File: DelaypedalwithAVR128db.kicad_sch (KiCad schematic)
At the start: 0 parts

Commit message: voltage bais
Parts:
- added C1: C, symbol Device:C
- added R1, R2: R, symbol Device:R
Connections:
- new net: C1.2, R1.2, R2.1
- new net Audio input: C1.1

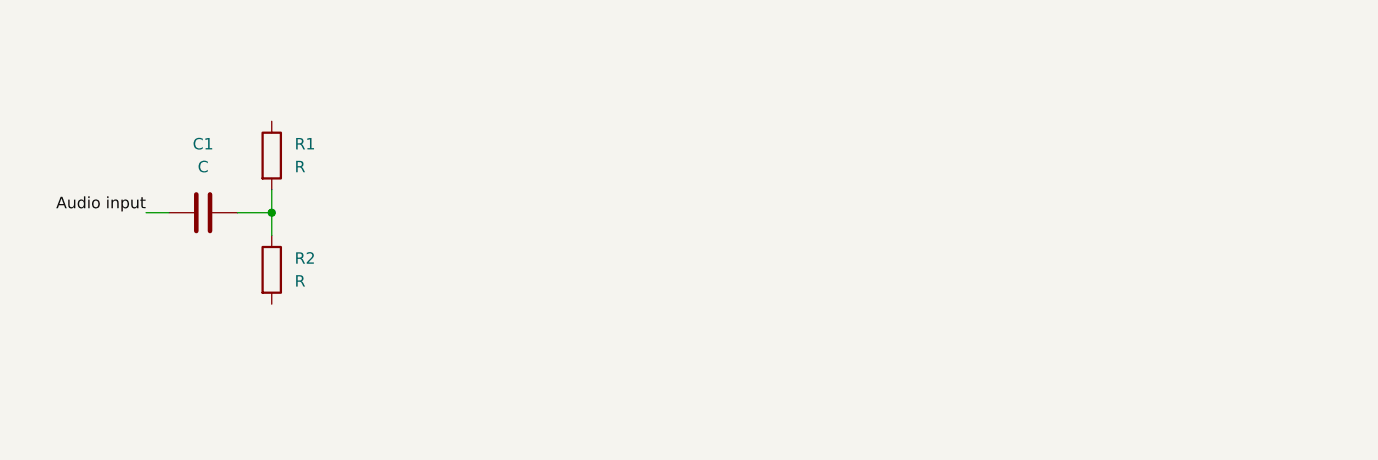
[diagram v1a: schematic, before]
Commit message: almost input stage done
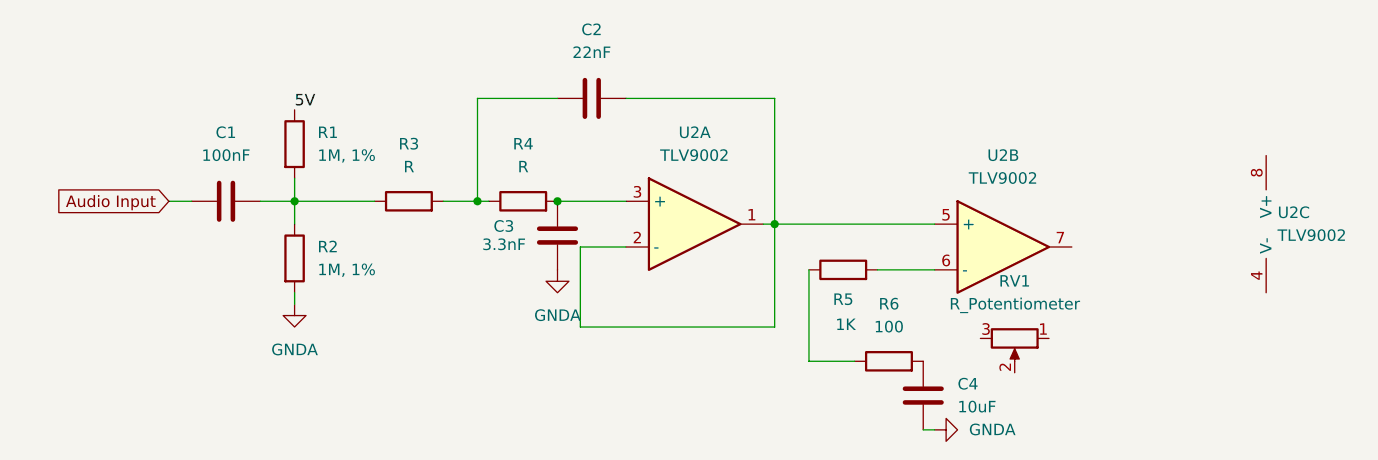
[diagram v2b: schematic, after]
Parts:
- added C2: 22nF, symbol Device:C
- added C3: 3.3nF, symbol Device:C
- added C4: 10uF, symbol Device:C
- added R3, R4: R, symbol Device:R
- added R5: 1K, symbol Device:R
- added R6: 100, symbol Device:R
- added RV1: R_Potentiometer, symbol Device:R_Potentiometer
- added U2: TLV9002, symbol Device:Opamp_Dual
- C1: value C -> 100nF
- R1, R2: value R -> 1M, 1%
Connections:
- net at C1.2, R1.2, R2.1: now also R3.1
- net 5V: now reaches R1.1
- net GNDA: now reaches R2.2
- net GNDA: now also C3.1, C4.1
- net Audio input renamed Audio Input
- new net: C2.1, R3.2, R4.1
- new net: C2.2, U2.1, U2.2 (-), U2.5 (+)
- new net: C3.2, R4.2, U2.3 (+)
- new net: C4.2, R6.2
- new net: R5.1, R6.1
- new net: R5.2, U2.6 (-)
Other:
- moved on the sheet: C1, R1, R2

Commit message: input stage finished and mixer stage
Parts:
- added C5, C6, C7, C8: 100nF, symbol Device:C
- added RV2: R_Potentiometer, symbol Device:R_Potentiometer
- added U1: TLV9002, symbol Device:Opamp_Dual
- RV1: value R_Potentiometer -> Potentiometer, 10K, linear
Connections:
- net GNDA: now also C6.2, C8.2
- net at U2.4 (V-): now also C6.1
- net at U2.8 (V+): now also C5.2
- net at R5.2, U2.6 (-): now also RV1.2, RV1.3
- net Dry positive signal: now reaches RV1.1
- net Dry positive signal: now also U2.7, RV2.1
- new net: C8.1, U1.4 (V-)
- new net: RV2.2, U1.3 (+)
- new net: C7.1, U1.8 (V+)
- new net 5VA: C5.1, C7.2
- new net Audio output: U1.1, U1.2 (-)
- new net Wet positive signal: RV2.3
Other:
- note added: "Input stage"
- note added: "Mixer"
- moved on the sheet: U2C

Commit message: fixed output maming
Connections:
- net Audio output renamed Audio ouput 1
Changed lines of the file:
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@@
+		)
+	)
+	(label "Audio ouput 1"
+		(at 66.04 127 0)
+		(effects
+			(font
+				(size 1.27 1.27)
+			)
+			(justify left bottom)
 		)
 	)
@@
 				(hide yes)
 			)
-		)
-	)
-	(global_label "Audio output"
-		(shape input)
-		(at 66.04 127 0)
-		(fields_autoplaced yes)
-		(effects
-			(font
-				(size 1.27 1.27)
-			)
-			(justify left)
-		)
-		(property "Intersheetrefs" "${INTERSHEET_REFS}"
-			(at 81.1806 127 0)
-			(effects
-				(font
-					(size 1.27 1.27)
-				)
-				(justify left)
-				(hide yes)
-			)

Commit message: added relay
yep thats it
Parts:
- added K1: Relay_SPDT, symbol Relay:Relay_SPDT
- R3, R4: value R -> 4,7K
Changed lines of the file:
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@@
 			)
 		)
-		(property "Value" "R"
+		(property "Value" "4,7K"
 			(at 54.61 69.85 90)
 			(effects
@@
 			)
 		)
-		(property "Value" "R"
+		(property "Value" "4,7K"
 			(at 67.31 69.85 90)
 			(effects
@@
 				)
 			)
+		)
+	)
+	(symbol
+		(lib_id "Relay:Relay_SPDT")
+		(at 41.91 161.29 0)
+		(unit 1)
+		(exclude_from_sim no)
+		(in_bom yes)
+		(on_board yes)
+		(dnp no)
+		(fields_autoplaced yes)
+		(property "Reference" "K1"
+			(at 53.34 160.0199 0)
+			(effects
+				(font
+					(size 1.27 1.27)
+				)
+				(justify left)
+			)
+		)
+		(property "Value" "Relay_SPDT"
+			(at 53.34 162.5599 0)
+			(effects
+				(font
+					(size 1.27 1.27)
+				)
+				(justify left)
+			)
+		)
+		(property "Footprint" ""
+			(at 53.34 162.56 0)
+			(effects
+				(font
+					(size 1.27 1.27)
+				)
+				(justify left)
+				(hide yes)
+			)
+		)
+		(property "Datasheet" "~"
+			(at 41.91 161.29 0)
+			(effects
+				(font
+					(size 1.27 1.27)
+				)
+				(hide yes)
+			)
+		)
+		(property "Description" "Relay SPDT, monostable, EN50005"
+			(at 41.91 161.29 0)
+			(effects
+				(font
+					(size 1.27 1.27)
+				)
+				(hide yes)
+			)
+		)
+		(pin "11"
+		)
+		(pin "14"
+		)
+		(pin "A1"
+		)
+		(pin "12"
+		)
+		(pin "A2"
+		)
+		(instances
+			(project ""
+				(path "/df84d36d-d6d4-4d90-9a88-48fc6a8fe70c"
+					(reference "K1")
+					(unit 1)
+				)
+			)

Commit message: bypass almost done
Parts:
- added C9: 10uF, symbol Device:C
- added J1, J2: NJ2FD-V, Connector_Audio:Jack_6.35mm_Neutrik_NJ2FD-V_Vertical, symbol Connector_Audio:NJ2FD-V
- added R7: 1M, symbol Device:R
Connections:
- net Dry positive signal: now also K1.12
- net GNDA: now also J1.S, J2.S, R7.1
- net at K1.11: now also C9.1
- net Audio output 1: now reaches K1.14
- net Audio Input renamed Audio input
- net Audio input: now also J1.T
- new net Audio outpu: C9.2, J2.T, R7.2
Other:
- note added: "Bypass"
- moved on the sheet: K1

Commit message: Bypass finished???
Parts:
- added C10: 10uF, PCM_JLCPCB:C_1206, symbol PCM_JLCPCB-Capacitors:1206,10uF
- added C11: 100nF, PCM_JLCPCB:C_1206, symbol PCM_JLCPCB-Capacitors:1206,100nF
- added D1: IN4148, symbol Device:D
- added Q1: BC847, Package_TO_SOT_SMD:SOT-23, symbol Transistor_BJT:BC847
- added R8: 1K, symbol Device:R
- added R9: 10K, symbol Device:R
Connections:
- net 5VA: now also K1.A1, C10.1, C11.1, D1.1 (K)
- net GNDA: now also C10.2, C11.2, Q1.3 (C), R9.1
- net at K1.A2: now also D1.2 (A), Q1.2 (E)
- new net: Q1.1 (B), R8.2, R9.2
- new net Bypass pin: R8.1
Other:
- moved on the sheet: C9, J2, K1

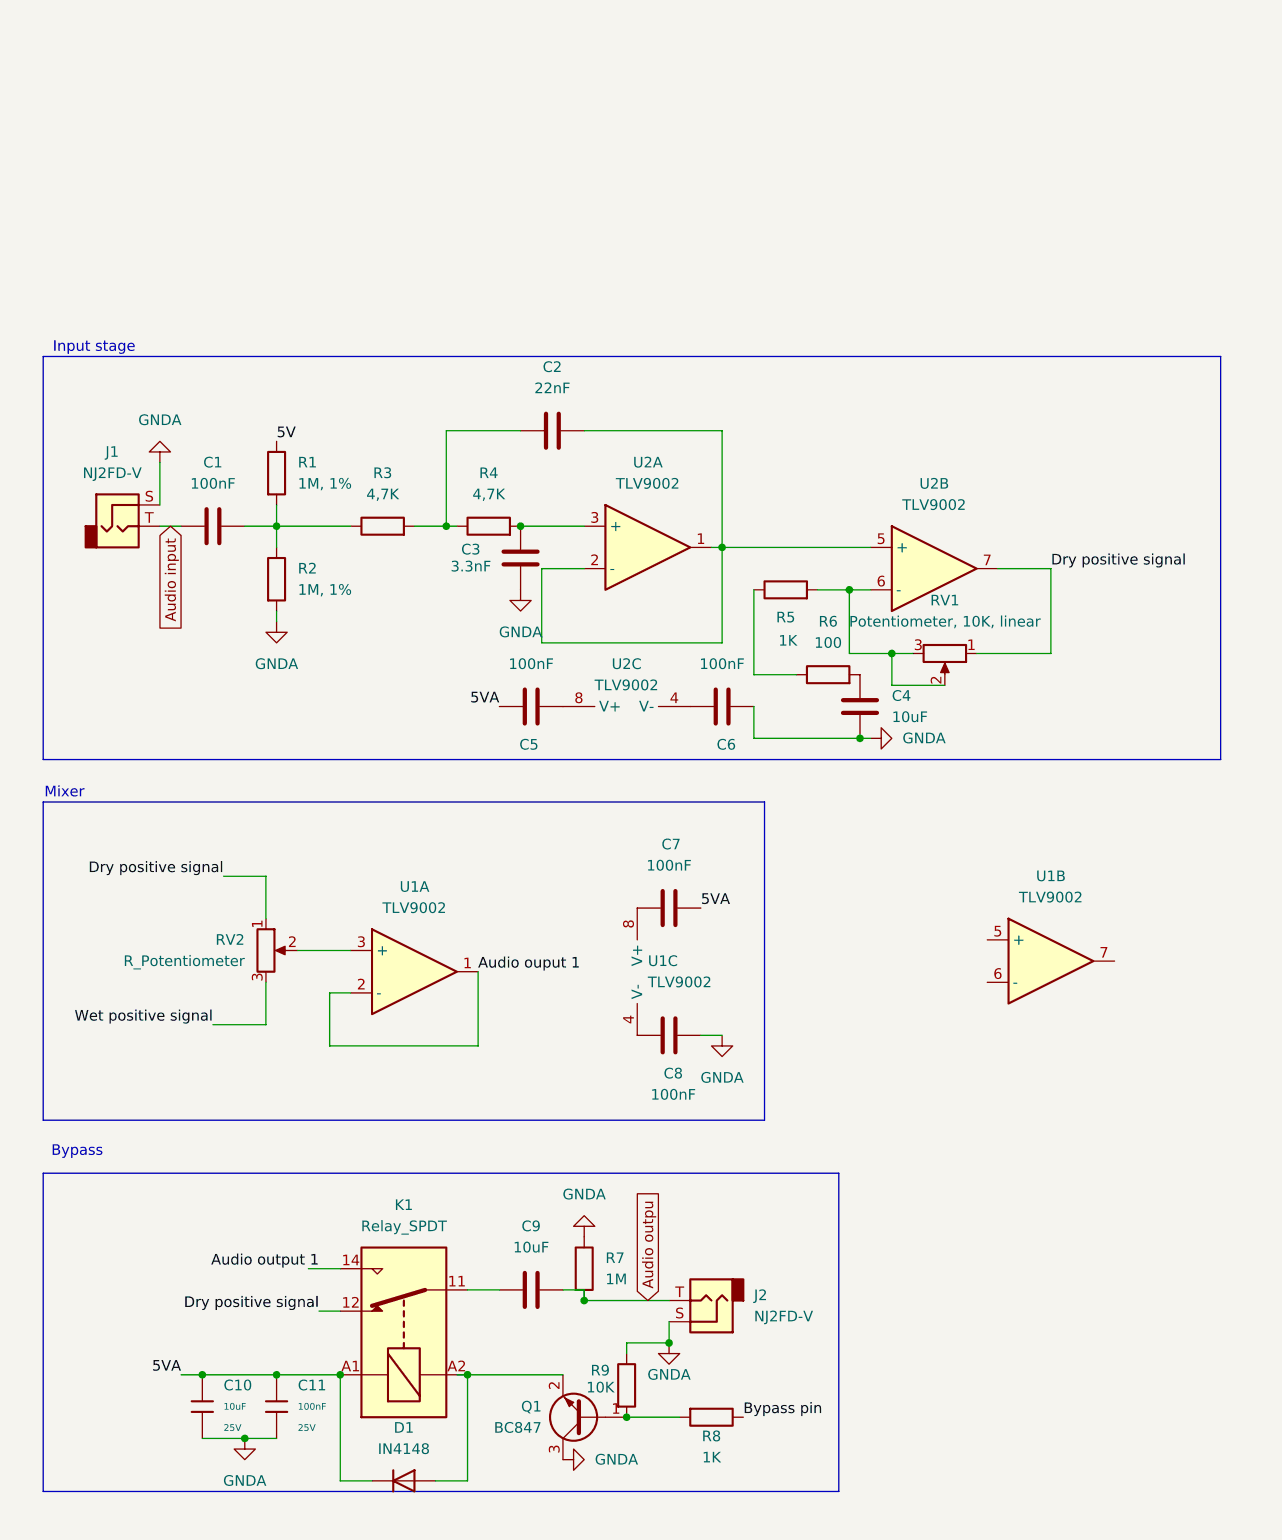
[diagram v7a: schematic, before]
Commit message: pin names fixed
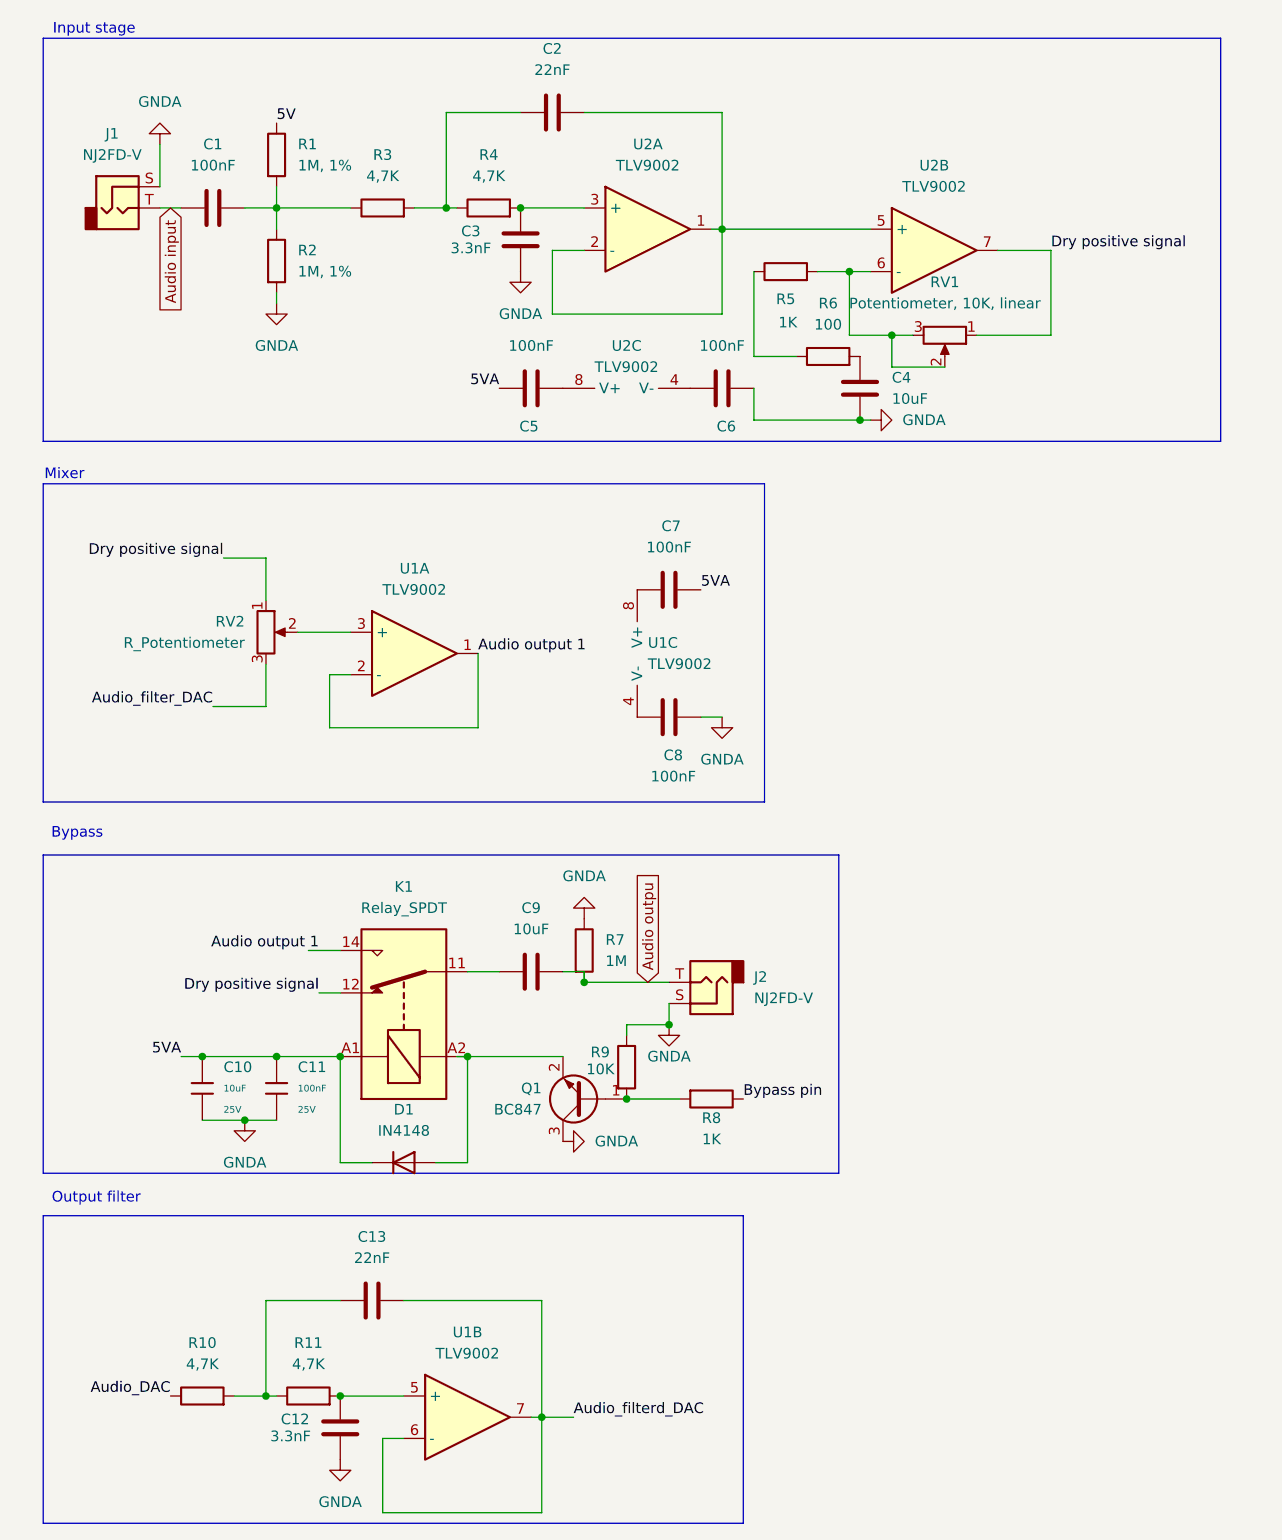
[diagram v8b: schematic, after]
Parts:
- added C12: 3.3nF, symbol Device:C
- added C13: 22nF, symbol Device:C
- added R10, R11: 4,7K, symbol Device:R
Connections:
- net Audio ouput 1 is gone; now on net Audio output 1: U1.1, U1.2 (-)
- net GNDA: now also C12.1
- net at U1.5 (+): now also C12.2, R11.2
- net Audio_filterd_DAC: now reaches U1.6 (-)
- net Audio_filterd_DAC: now also U1.7, C13.2
- net Wet positive signal renamed Audio_filter_DAC
- new net: C13.1, R10.2, R11.1
- new net Audio_DAC: R10.1
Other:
- note added: "Output filter"
- moved on the sheet: C1, C10, C11, C2, C3, C4, C5, C6, C7, C8, C9, D1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
